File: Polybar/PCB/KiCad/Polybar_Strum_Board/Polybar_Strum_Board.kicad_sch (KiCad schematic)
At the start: 15 parts, among them J1 Conn_01x09_Pin, SW1 MX_SW_solder, SW2 MX_SW_solder, SW3 MX_SW_solder, SW4 MX_SW_HS, SW5 MX_SW_HS, U1 ProMicro, U2 RKJXV1224005

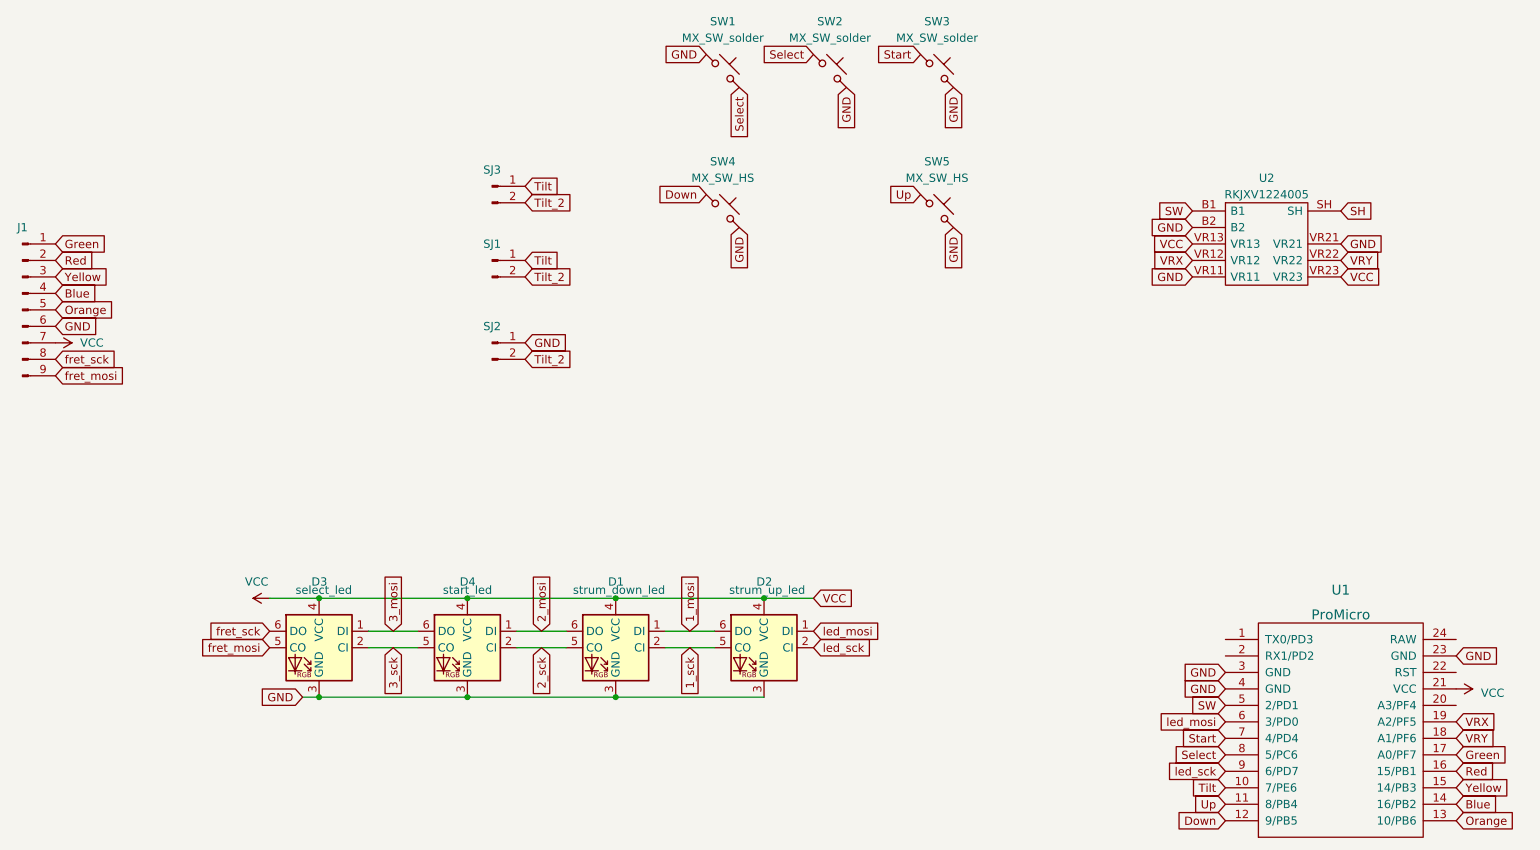
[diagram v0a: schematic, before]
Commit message: Deleted extra footprints and updated Schematic
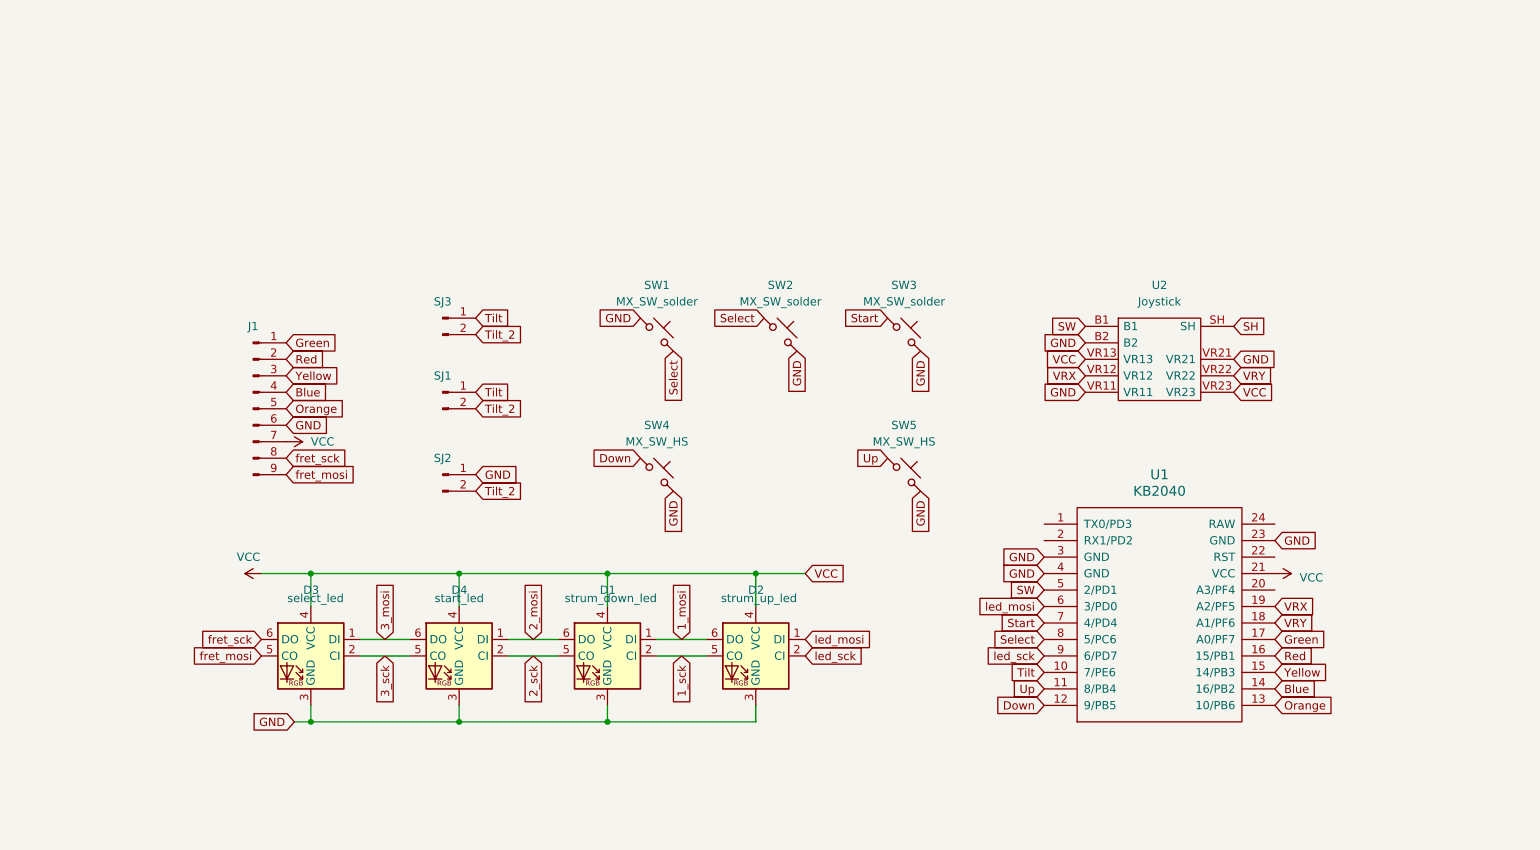
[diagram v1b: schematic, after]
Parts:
- removed U1: ProMicro, Polybar:KB2040-ProMicroPins, symbol keebio:ProMicro
- removed U2: RKJXV1224005, RKJXV1224005, symbol Polybar:RKJXV1224005
- added U1: KB2040, Minibar:KB2040, symbol Minibar:KB2040
- added U2: Joystick, Minibar:Joystick, symbol Minibar:Joystick
- SJ1: footprint Polybar:Solder_Jumper -> Minibar:Solder_Jumper
- SW4, SW5: footprint Polybar:Kailh_Hotswap_MX -> Minibar:Kailh_Hotswap_MX
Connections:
- net Blue: now also U1.14 (16/PB2)
- net Down: now also U1.12 (9/PB5)
- net GND: now also U1.23 (GND), U1.3 (GND), U1.4 (GND), U2.B2, U2.VR11, U2.VR21
- net Green: now also U1.17 (A0/PF7)
- net Orange: now also U1.13 (10/PB6)
- net Red: now also U1.16 (15/PB1)
- net SH: now also U2.SH
- net SW: now also U1.5 (2/PD1), U2.B1
- net Select: now also U1.8 (5/PC6)
- net Start: now also U1.7 (4/PD4)
- net Tilt: now also U1.10 (7/PE6)
- net Up: now also U1.11 (8/PB4)
- net VCC: now also U1.21 (VCC), U2.VR13, U2.VR23
- net VRX: now also U1.19 (A2/PF5), U2.VR12
- net VRY: now also U1.18 (A1/PF6), U2.VR22
- net Yellow: now also U1.15 (14/PB3)
- net led_mosi: now also U1.6 (3/PD0)
- net led_sck: now also U1.9 (6/PD7)
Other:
- moved on the sheet: D1, D2, D3, D4, J1, SJ1, SJ2, SJ3, SW1, SW2, SW3, SW4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
